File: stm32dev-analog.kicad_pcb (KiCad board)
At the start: 2 copper layers, 53.3 x 72.4 mm, 56 parts, among them J3 Conn_01x20_Male, J4 Conn_01x20_Male, J8 Conn_02x08_Odd_Even, Q1 LBSS84LT1G, Q2 2N7002, U1 TL072, U2 TL072, U3 TL072, U4 74LVC1T45W6, U5 TL072

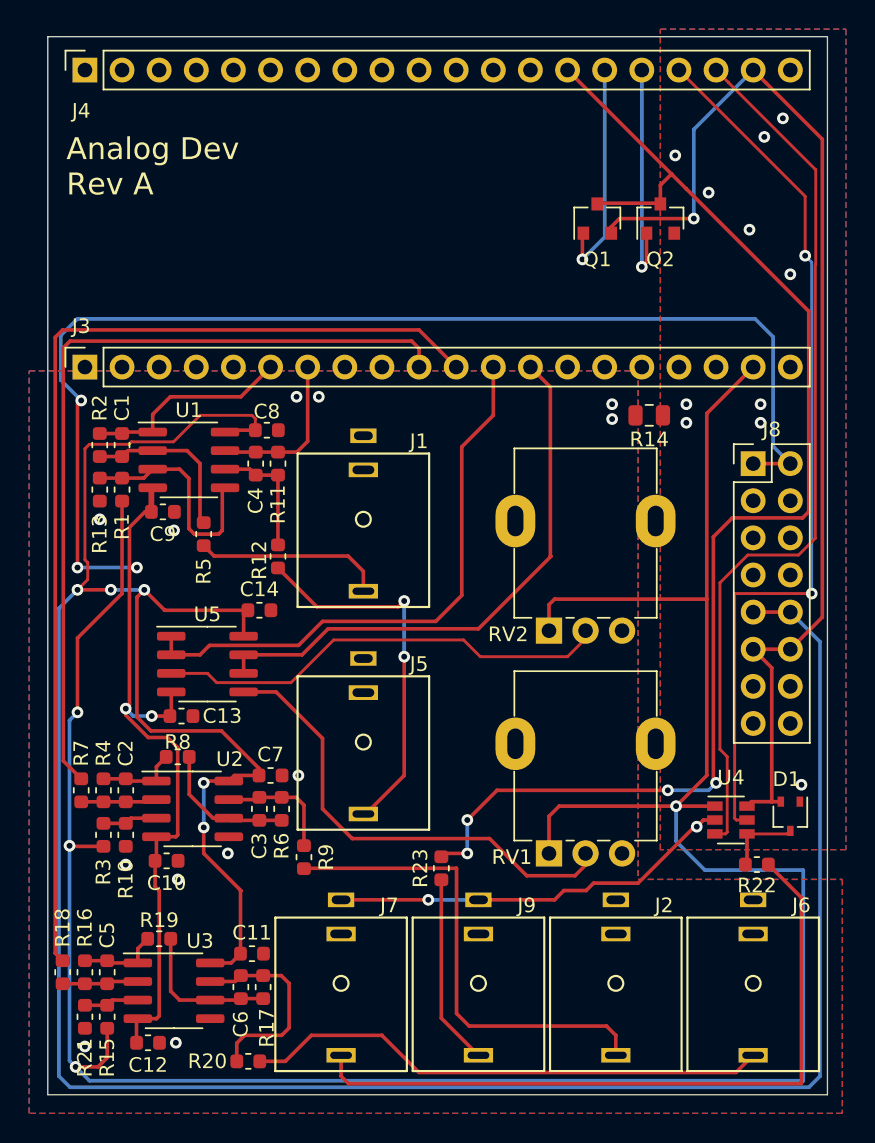
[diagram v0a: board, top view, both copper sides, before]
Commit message: Changed BAT54 to discrete diodes to use Basic instead of Extended part.
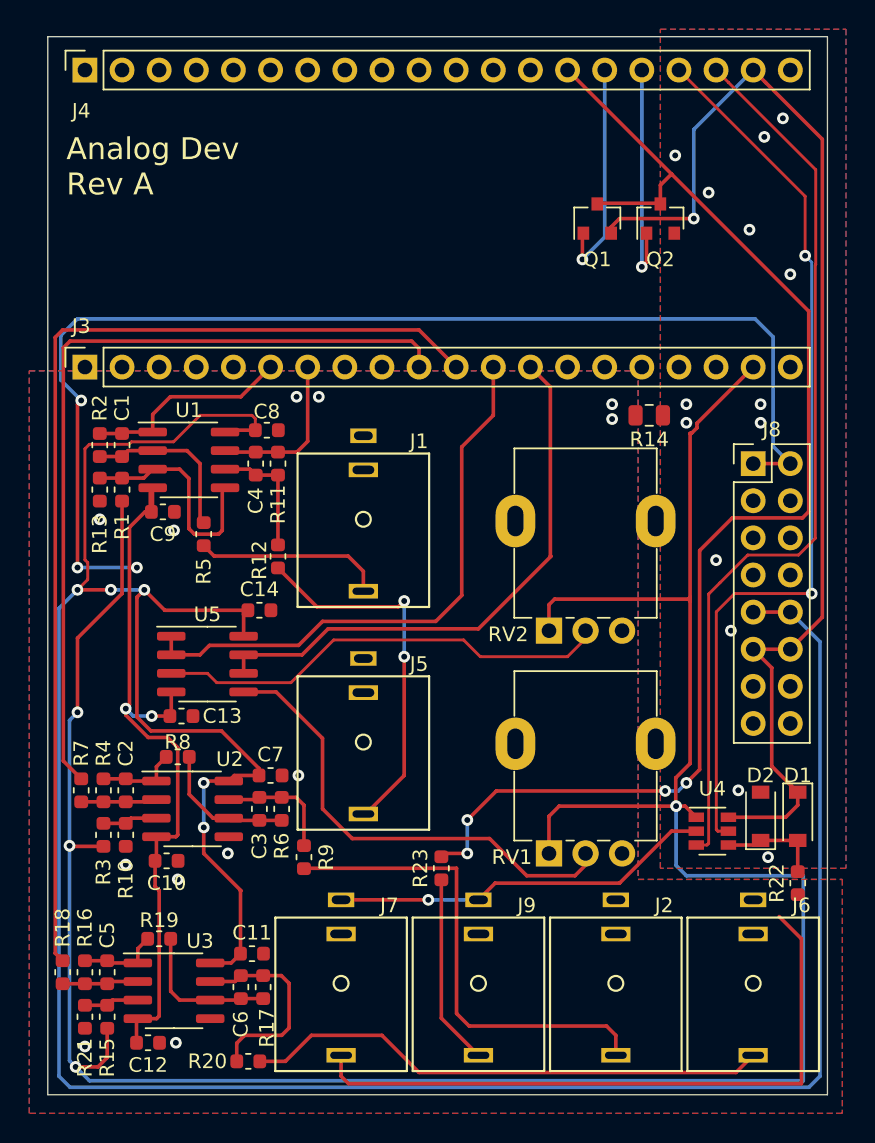
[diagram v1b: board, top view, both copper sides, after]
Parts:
- added D2: B5819W, Diode_SMD:D_SOD-123, F.Cu at (151.6, 80.0)
- D1: value BAT54SW -> B5819W; footprint Package_TO_SOT_SMD:SOT-323_SC-70 -> Diode_SMD:D_SOD-123
- moved R22 3.07 mm to (154.2, 84.6), turned to 90 degrees
- moved U4 1.48 mm to (148.3, 81.0)
- moved D1 0.51 mm to (154.2, 80.0)
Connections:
- D1 pad 1: GNDD -> +5V
- D1 pad 2: +5V -> Net-(D1-Pad2)
- R22 pad 2: Net-(D1-Pad3) -> Net-(D1-Pad2)
- U4 pad 4: Net-(D1-Pad3) -> Net-(D1-Pad2)
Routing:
- net Net-(D1-Pad2): track 0.00 -> 7.01 mm
- net Net-(D1-Pad3): track 5.19 -> 0.00 mm
- net Net-(J7-PadT): track 49.1 -> 45.2 mm
- net +5V: track 76.6 -> 80.2 mm
- net GNDD: track 27.8 -> 26.2 mm, vias 13 -> 15
- net PB14: track 90.1 -> 88.7 mm
- net PB11: track 61.1 -> 62.4 mm
- net +3V3: track 182.8 -> 181.8 mm
- net PB10: track 60.8 -> 61.7 mm
